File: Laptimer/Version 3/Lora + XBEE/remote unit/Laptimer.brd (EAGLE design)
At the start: 100 x 75 mm, 33 parts, among them IC4 74HC04D, IC5 NE555D, X2 GLX-S-88M

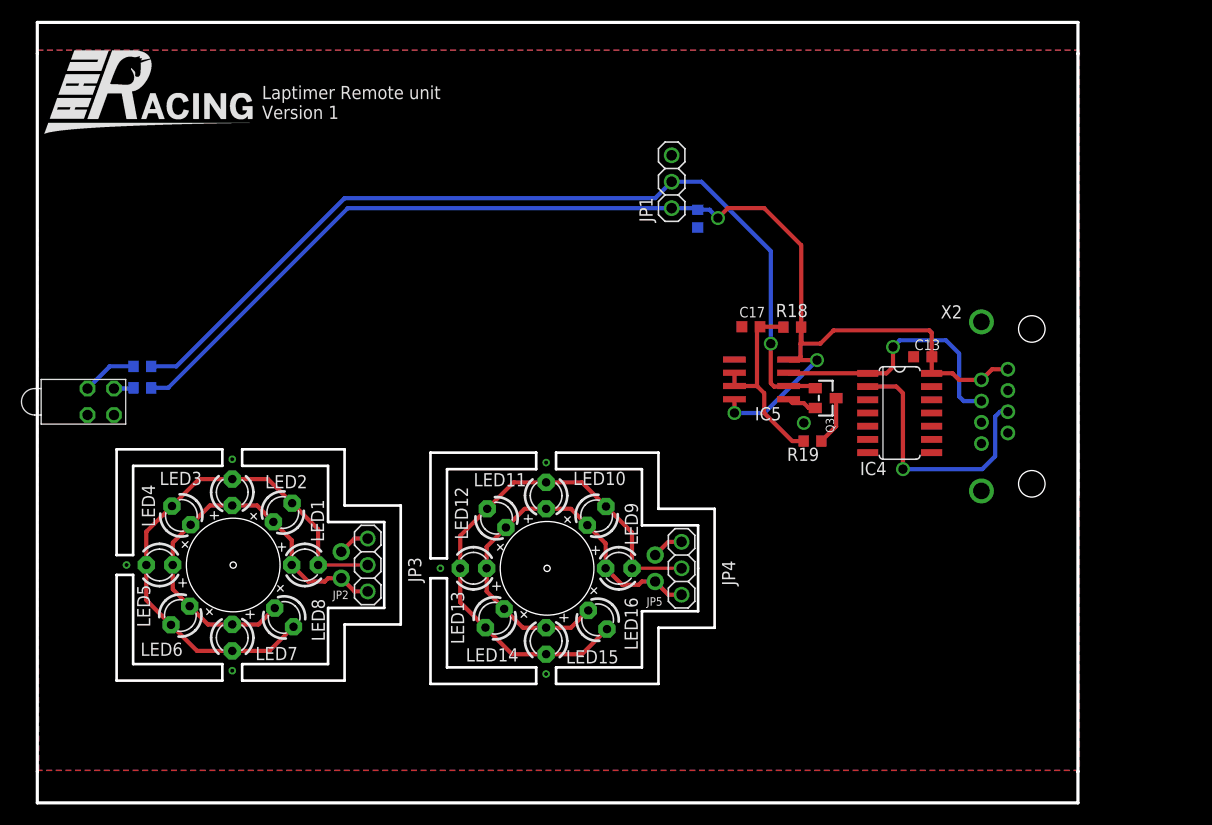
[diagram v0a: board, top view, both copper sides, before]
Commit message: laptimer RC done, com node (done) need checkup
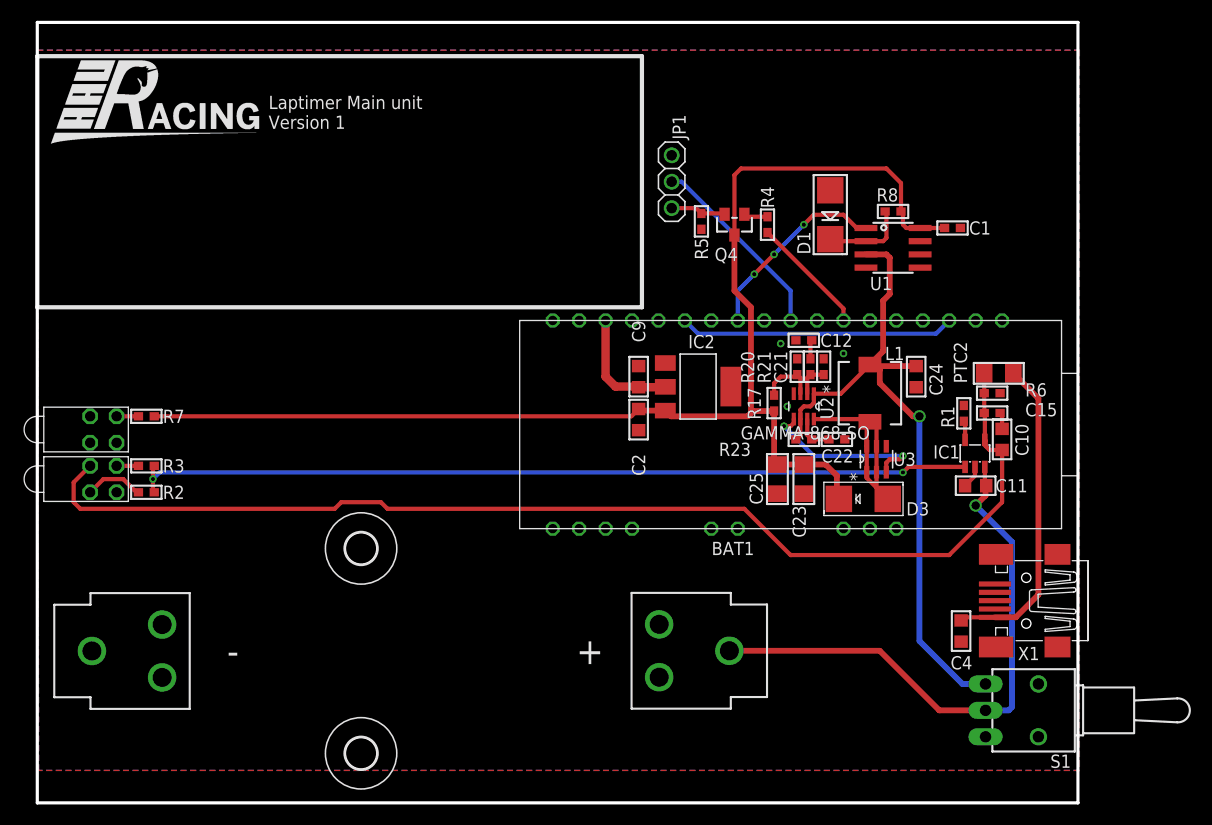
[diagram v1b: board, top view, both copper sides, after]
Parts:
- removed C13, C17: 100n, rcl:C0603K
- removed IC4: 74HC04D, 74xx-eu:SO14
- removed IC5: NE555D, linear:SO08
- removed JP2, JP5: (no value), microbuilder:1X02_ROUND
- removed JP3, JP4: (no value), adafruit:1X03
- removed LED1, LED10, LED11, LED12, LED13, LED14, LED15, LED16, LED2, LED3, LED4, LED5, LED6, LED7, LED8, LED9: SFH 309, adafruit:LED3MM
- removed Q3: (no value), microbuilder:SOT23-WIDE
- removed R15, R16: 220, rcl:R0603
- removed R18: 1k, rcl:R0603
- removed R19: 100, rcl:R0603
- removed U$19: BI-LEVEL-LED-INDICATOR, unicorn_v2:BI-LEVEL-LED-INDICATOR
- removed X2: GLX-S-88M, con-kycon:GLX-S-88M
- added BAT1: (no value), SparkFun-Electromechanical:BATTERY_18650-HOLDER
- added C1, C15: 100n, microbuilder:_0603
- added C10, C11, C2, C24: 10u, microbuilder:_0805
- added C12: 1n8, microbuilder:_0603
- added C21: 47p, microbuilder:_0603
- added C22: 1n, microbuilder:_0603
- added C23, C25: 100u, microbuilder:1206
- added C4, C9: 22u, microbuilder:_0805
- added D1: 3V, microbuilder:SMADIODE
- added D3: B320, adafruit:SMADIODE
- added H1, H2: MOUNT-HOLE3.0, holes:3,0
- added IC1: MCP73831/OT, adafruit:SOT23-5L
- added IC2: REG1117, burr-brown:SOT223
- added L1: FDVE0630-H-1R0M, microbuilder:INDUCTOR_6X6MM_TDK_SLF6045
- added PTC2: (no value), microbuilder:1206
- added Q4: PBSS4120T, microbuilder:SOT23-WIDE
- added R1, R8: 2k, microbuilder:_0603
- added R17: 34k8, microbuilder:_0603
- added R2: 470, microbuilder:_0603
- added R20: 11k, microbuilder:_0603
- added R21: 17k4, microbuilder:_0603
- added R23: 1m, microbuilder:_0603
- added R3, R4: 1k, microbuilder:_0603
- added R6: 10k, microbuilder:_0603
- added R7: 220, microbuilder:_0603
- added S1: TL36WO, switch:TL3XWO
- added U$13, U$14: BI-LEVEL-LED-INDICATOR, unicorn_v2:BI-LEVEL-LED-INDICATOR
- added U$7: GAMMA-868-SO, unicorn_v2:UNICORN_V2_GAMMA-868-SO
- added U1: (no value), microbuilder:SOIC8_150MIL
- added U2: LTC3872ETS8TRMPBF, LTC_By_element14_Batch_1:SOT65P280X100-8N
- added U3: SI3460DDV-T1-GE3, Vishay_By_element14_Batch_1:SOT95P285X110-6N
- added X1: mini-usb, con-cypressindustries:32005-301
- R5: device rcl:R0603 -> microbuilder:_0603
- moved R5 0.44 mm to (63.8, 55.9), flipped to the top
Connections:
- removed net INT: JP3.2, LED1.K, LED2.K, LED3.K, LED4.K, LED5.K, LED6.K, LED7.K, LED8.K
- removed net INT1: JP4.2, LED10.K, LED11.K, LED12.K, LED13.K, LED14.K, LED15.K, LED16.K, LED9.K
- removed net N$10: JP2.1, JP3.1
- removed net N$22: IC4.2, X2.5
- removed net N$25: R15.2, U$19.ANODE1
- removed net N$36: C17.1, IC5.6, IC5.7, R18.2, R19.2
- removed net N$40: JP2.2, JP3.3, LED1.A, LED2.A, LED3.A, LED4.A, LED5.A, LED6.A, LED7.A, LED8.A
- removed net N$41: Q3.3, R19.1
- removed net PT-OUT: IC4.1, IC5.3, X2.4
- new net +UB: C10.2, C15.1, IC1.4, PTC2.1, R6.1, U$13.ANODE1
- new net 3.3V: C9.1, IC2.2, U$7.P$16
- new net BAT-ADC: BAT1.PWR@1, C11.1, IC1.3, S1.2
- new net CHRG-DONE-LED: R3.1, U$13.ANODE2
- new net CT: U$7.P$13, U$7.P$3
- new net LASER: R4.1, U$7.P$7
- new net MOSD: D3.A, L1.P$1, U2.8, U3.1, U3.2, U3.5, U3.6
- new net N$1: R17.2, R20.1, U2.3
- new net N$13: C4.1, PTC2.2, X1.1
- new net N$14: R2.1, U$13.CATHODE1
- new net N$2: C12.2, R21.2
- new net N$27: C21.2, R21.1, U2.2
- new net N$29: C22.2, R23.1, U2.7
- new net N$3: IC1.5, R1.1
- new net N$4: IC1.1, R2.2, R3.2
- new net N$5: JP1.1, Q4.2, R5.1
- new net N$6: Q4.1, R4.2
- new net RLB: U$7.P$11, U1.1
- new net VBAT: C24.2, L1.P$2, R23.2, S1.1, U1.3, U2.1, U2.6
- net 5.0V: now also C1.1, C2.1, C23.1, C25.1, D3.C, IC2.3, Q4.3, R17.1, R7.1, R8.1, U1.8; no longer C13.2, IC4.14, IC5.4, IC5.8, JP1.1, R16.1, R18.1, R5.1, X2.1, X2.2
- net GND: now also BAT1.GND@1, C1.2, C10.1, C11.2, C12.1, C15.2, C2.2, C21.1, C22.1, C23.2, C24.1, C25.2, C4.2, C9.2, D1.A, IC1.2, IC2.1, R1.2, R20.2, R6.2, U$13.CATHODE2, U$14.CATHODE1, U$14.CATHODE2, U$7.P$10, U$7.P$15, U$7.P$2, U1.4, U2.4, U3.4, X1.5, X1.M1, X1.M2, X1.M3, X1.M4; no longer C13.1, C17.2, IC4.11, IC4.13, IC4.3, IC4.5, IC4.7, IC4.9, IC5.1, Q3.2, U$19.CATHODE1, U$19.CATHODE2, X2.3, X2.6, X2.7, X2.8, X2.S1, X2.S2
- net N$32: now also R7.2, U$14.ANODE2; no longer R16.2, U$19.ANODE2
- net N$7: now also D1.C, R8.2, U1.2; no longer JP4.1, JP5.1
- net N$8: now also U2.5, U3.3; no longer JP4.3, JP5.2, LED10.A, LED11.A, LED12.A, LED13.A, LED14.A, LED15.A, LED16.A, LED9.A
- net PT-IN: now also U$7.P$9; no longer IC5.2, Q3.1, R15.1
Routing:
- net +UB: track 0.00 -> 111.9 mm
- net N$4: track 0.00 -> 81.2 mm, vias 1 -> 2
- net PT-IN: track 86.9 -> 18.6 mm, vias 1 -> 0
- net VBAT: track 0.00 -> 66.6 mm, vias 0 -> 1
- net BAT-ADC: track 0.00 -> 54.7 mm, vias 0 -> 1
- net INT: track 52.5 -> 0.00 mm
- net INT1: track 52.4 -> 0.00 mm
- net N$40: track 41.6 -> 0.00 mm
- net N$13: track 0.00 -> 30.9 mm
- net CT: track 0.00 -> 26.5 mm
- net PT-OUT: track 25.8 -> 0.00 mm, vias 1 -> 0
- net N$22: track 25.6 -> 0.00 mm, vias 1 -> 0
- net N$8: track 41.5 -> 16.9 mm, vias 0 -> 2
- net MOSD: track 0.00 -> 21.2 mm
- net N$36: track 19.3 -> 0.00 mm
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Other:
- outline, holes or cut-outs redrawn
- board text added: "Laptimer Main unit Version 1"
- board text removed: "Laptimer Remote unit Version 1"
